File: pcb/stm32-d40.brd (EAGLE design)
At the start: 57.1 x 17.8 mm, 33 parts, among them IC1 TODO AMIS30663CANG2G, IC2 STM32F103C8, J1 DIP-40, Q2 8MHz, SW1 KSS-2EG4430, SW2 KSS-2EG4430, X1 DG3XX-03-3.5

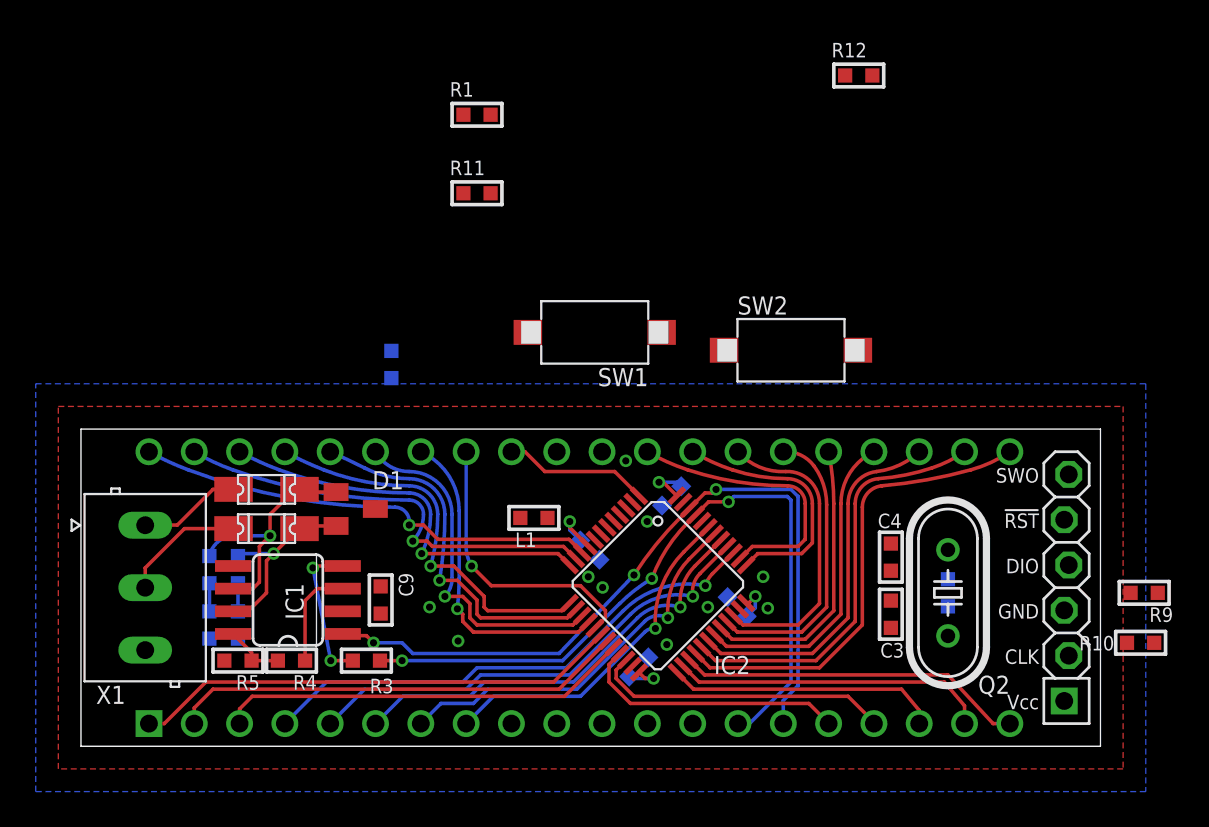
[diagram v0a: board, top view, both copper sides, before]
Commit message: DIP40 CAN ready
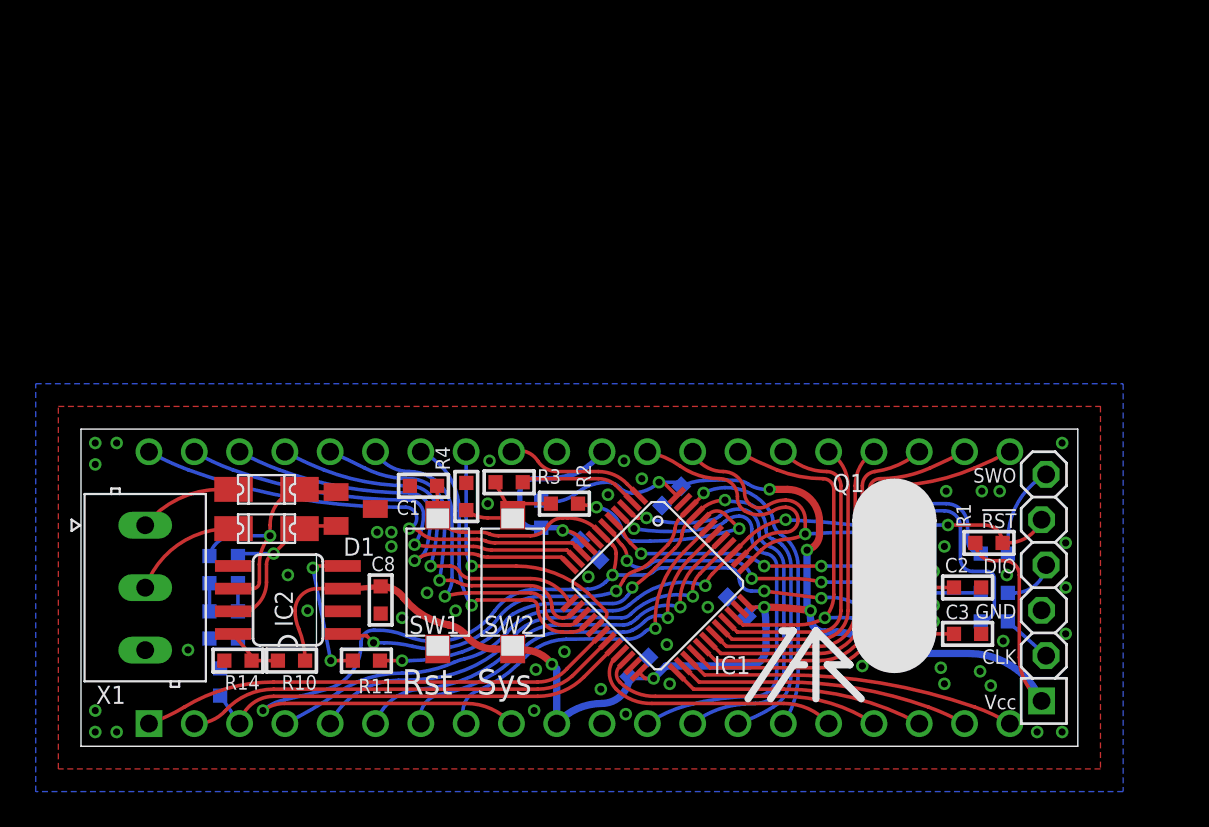
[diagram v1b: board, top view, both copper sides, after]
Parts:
- removed C11: 560pF, rc-master-smd:C0603
- removed Q2: 8MHz, discrete:HC49/S
- added C1: 0.1, rc-master-smd:C0603
- added C2: 22pF, rc-master-smd:C0603
- added Q1: 8MHz, discrete:HC49/S
- added R13: 100, rc-master-smd:R0603
- added R14: NC, rc-master-smd:R0603
- added U$: LOGO, logo:TT_LOGO
- C4: value 22pF -> 0.1
- C9: value 0.1 -> 560pF
- IC1: value TODO AMIS30663CANG2G -> STM32F103C8; device interfaces:SO08 -> stm32:LQFP48
- IC2: value STM32F103C8 -> TODO AMIS30663CANG2G; device stm32:LQFP48 -> interfaces:SO08
- R10: value 10K -> 0
- R11: value 2.2K -> 100
- R12, R8, R9: value 10K -> 100
- R2: value 1M -> 10K
- R3, R6: value 100 -> 10K
- R4: value 0 -> 2.2K
- R5: value NC -> 1M
- moved R10 47.6 mm to (11.8, 4.80)
- moved R12 44.5 mm to (8.80, 9.90), flipped to the bottom, turned to 90 degrees
- moved R7 44.1 mm to (51.2, 7.00), turned to 180 degrees
- moved R1 37.4 mm to (50.9, 11.4), turned to 180 degrees
- moved R5 37.1 mm to (45.6, 9.60), flipped to the bottom, turned to 270 degrees
- moved R8 36.1 mm to (51.2, 8.60), turned to 180 degrees
- moved R11 26.9 mm to (16.0, 4.80), turned to 180 degrees
- moved R2 22.1 mm to (27.1, 13.6), flipped to the top, turned to 0 degrees
- moved IC1 20.8 mm to (32.3, 9.09), turned to 225 degrees
- moved IC2 20.8 mm to (11.6, 8.20), turned to 90 degrees
- moved SW2 20.3 mm to (24.2, 9.20), turned to 90 degrees
- moved C8 17.3 mm to (16.8, 8.20), flipped to the top, turned to 270 degrees
- moved C4 16.9 mm to (28.5, 11.0), flipped to the bottom, turned to 225 degrees
- moved SW1 16.5 mm to (20.0, 9.20), turned to 90 degrees
- moved R4 13.4 mm to (21.6, 14.0), turned to 270 degrees
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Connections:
- new net N$2: R7.2, SWD1.2
- new net N$3: R8.2, SWD1.4
- new net N$4: R9.2, SWD1.6
- net !RESET: now also C1.1, IC1.7, R1.1; no longer IC2.7, R12.1
- net +3V3: now also C7.1, IC1.24, IC1.36, IC1.48, IC2.3, R1.2, R10.1; no longer C9.1, IC1.3, IC2.24, IC2.36, IC2.48, R10.2, R12.2, R4.1, R9.2
- net AVCC: now also C4.1, IC1.9; no longer C7.1, IC2.9
- net BOOT0: now also IC1.44, R2.2; no longer IC2.44, R1.2
- net CAN_CTRL: now also IC2.8, R10.2, R14.2; no longer IC1.8, R4.2, R5.2
- net GND: now also C1.2, C2.2, IC1.23, IC1.35, IC1.47, IC1.8, IC2.2, R14.1, R4.1, R6.2; no longer C11.2, IC1.2, IC2.23, IC2.35, IC2.47, IC2.8, R11.1, R5.1, R8.2
- net N$1: now also R2.1, R3.1, R4.2; no longer R1.1, R11.2
- net N$51: now also IC2.7, R12.2; no longer IC1.7, R6.2
- net N$52: now also IC2.6, R13.2; no longer IC1.6, R7.2
- net N$54: now also C10.1, R13.1; no longer C11.1, R7.1
- net N$55: now also C9.1, R12.1; no longer C10.1, R6.1
- net N$7: now also IC2.4, R11.2; no longer IC1.4, R3.2
- net OSC_IN: now also C2.1, IC1.5, Q1.1, R5.1; no longer C3.1, IC2.5, Q2.1, R2.1
- net OSC_OUT: now also C3.1, IC1.6, Q1.2, R5.2; no longer C4.1, IC2.6, Q2.2, R2.2
- net PA0: now also IC1.10; no longer IC2.10
- net PA1: now also IC1.11; no longer IC2.11
- net PA10/RXD1: now also IC1.31; no longer IC2.31
- net PA11/USBDM: now also IC1.32; no longer IC2.32
- net PA12/USBDP: now also IC1.33; no longer IC2.33
- net PA13/SWDIO: now also IC1.34, R8.1; no longer IC2.34, SWD1.4
- net PA14/SWCLK: now also IC1.37, R7.1; no longer IC2.37, SWD1.2
- net PA15: now also IC1.38; no longer IC2.38
- net PA2: now also IC1.12; no longer IC2.12
- net PA3: now also IC1.13; no longer IC2.13
- net PA4: now also IC1.14; no longer IC2.14
- net PA5: now also IC1.15; no longer IC2.15
- net PA6: now also IC1.16; no longer IC2.16
- net PA7: now also IC1.17; no longer IC2.17
- net PA8: now also IC1.29; no longer IC2.29
- net PA9/TXD1: now also IC1.30; no longer IC2.30
- net PB0: now also IC1.18; no longer IC2.18
- net PB1: now also IC1.19; no longer IC2.19
- net PB10: now also IC1.21; no longer IC2.21
- net PB11: now also IC1.22; no longer IC2.22
- net PB12: now also IC1.25; no longer IC2.25
- net PB13: now also IC1.26; no longer IC2.26
- net PB14: now also IC1.27; no longer IC2.27
- net PB15: now also IC1.28; no longer IC2.28
- net PB2: now also IC1.20, R6.1; no longer IC2.20, R8.1
- net PB3/SWO: now also IC1.39, R9.1; no longer IC2.39, SWD1.6
- net PB4: now also IC1.40; no longer IC2.40
- net PB5: now also IC1.41; no longer IC2.41
- net PB6/SCL1: now also IC1.42; no longer IC2.42, R9.1
- net PB7/SDA1: now also IC1.43; no longer IC2.43, R10.1
- net PB8/CANRX: now also IC1.45, R11.1; no longer IC2.45, R3.1
- net PB9/CANTX: now also IC1.46, IC2.1; no longer IC1.1, IC2.46
- net PC13: now also IC1.2, R3.2; no longer IC2.2
- net PC14/OSC32_IN: now also IC1.3; no longer IC2.3
- net PC15/OSC32_OUT: now also IC1.4; no longer IC2.4
- net VBAT: now also IC1.1; no longer IC2.1
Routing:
- net !RESET: track 0.00 -> 81.8 mm, vias 0 -> 5
- net +3V3: track 12.8 -> 92.7 mm, vias 3 -> 7
- net PC15/OSC32_OUT: track 0.00 -> 24.8 mm, vias 0 -> 1
- net OSC_IN: track 0.00 -> 24.1 mm, vias 0 -> 3
- net OSC_OUT: track 0.00 -> 23.3 mm, vias 0 -> 3
- net PC14/OSC32_IN: track 0.00 -> 22.9 mm, vias 0 -> 1
- net PB3/SWO: track 28.9 -> 44.1 mm, vias 1 -> 2
- net PA14/SWCLK: track 14.0 -> 28.7 mm, vias 0 -> 1
- net PA13/SWDIO: track 16.6 -> 29.3 mm, vias 0 -> 1
- net BOOT0: track 0.00 -> 12.4 mm, vias 0 -> 2
- net AVCC: track 3.14 -> 12.2 mm
- net N$1: track 0.00 -> 7.79 mm
- net PC13: track 0.00 -> 6.71 mm
- net N$4: track 0.00 -> 5.02 mm
- net PB9/CANTX: track 43.3 -> 40.3 mm
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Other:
- board size 57.1 x 17.8 mm -> 55.9 x 17.8 mm
- board text added: "!RST"
- board text added: "+3V3"
- board text added: "AVCC"
- board text added: "CAN"
- board text added: "CANARM"
- board text added: "GND"
- board text added: "H+"
- board text added: "L-"
- board text added: "PA0"
- board text added: "PA1"
- board text added: "PA10"
- board text added: "PA11"
- board text added: "PA12"
- board text added: "PA13"
- board text added: "PA14"
- board text added: "PA15"
- board text added: "PA2"
- board text added: "PA3"
- board text added: "PA4"
- board text added: "PA5"
- board text added: "PA6"
- board text added: "PA7"
- board text added: "PA8"
- board text added: "PA9"
- board text added: "PB0"
- board text added: "PB1"
- board text added: "PB10"
- board text added: "PB11"
- board text added: "PB12"
- board text added: "PB13"
- board text added: "PB14"
- board text added: "PB15"
- board text added: "PB2"
- board text added: "PB3"
- board text added: "PB4"
- board text added: "PB5"
- board text added: "PB6"
- board text added: "PB7"
- board text added: "PB8"
- board text added: "PB9"
- board text added: "PC14"
- board text added: "PC15"
- board text added: "Rev.13A"
- board text added: "Rst"
- board text added: "Sys"
- board text added: "Vbat"
- board text added: "i@tuxotronic.org"

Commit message: some wire fixes, add LED
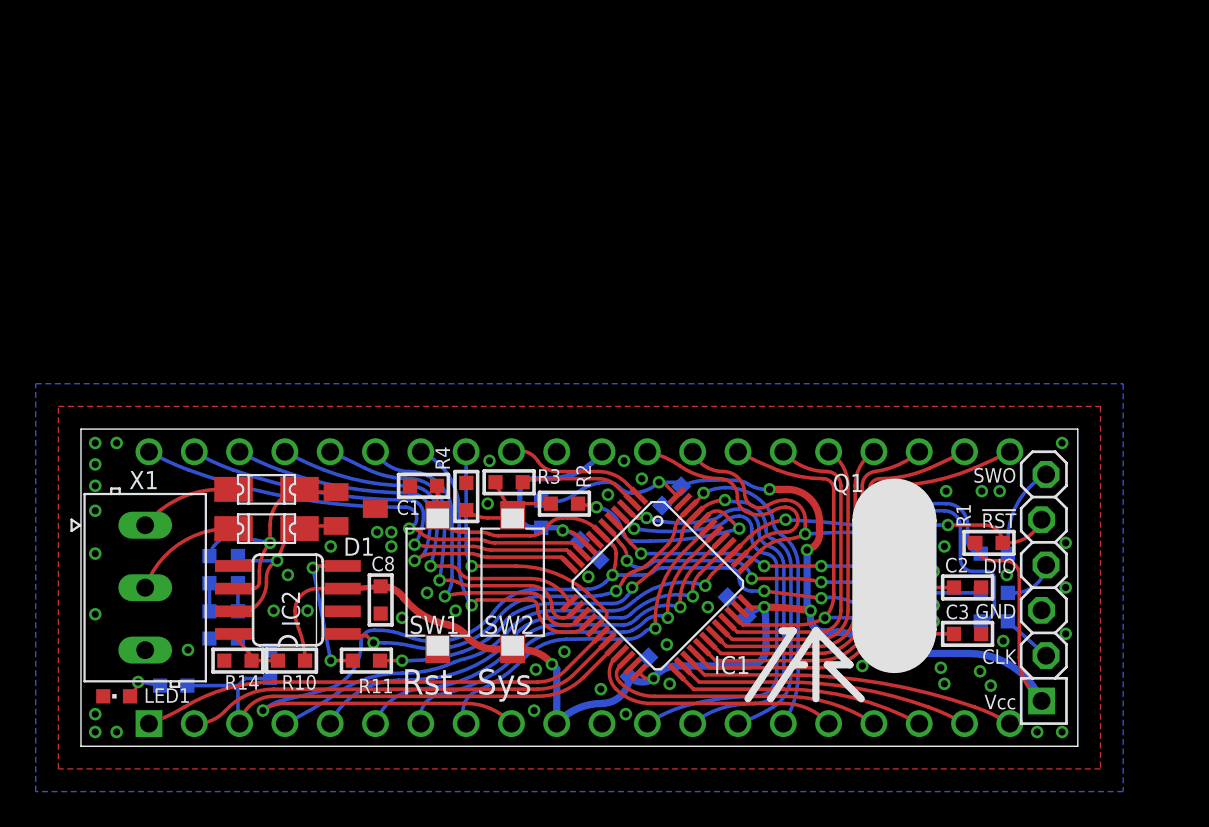
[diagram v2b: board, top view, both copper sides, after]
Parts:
- added LED1: (no value), led:CHIPLED_0603
- added R15: 330, rc-master-smd:R0603
- moved R6 2.97 mm to (10.6, 4.60)
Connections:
- new net N$5: LED1.A, R15.2
- net GND: now also LED1.C
- net PB2: now also R15.1
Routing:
- net PB2: track 24.3 -> 29.4 mm
- net N$5: track 0.00 -> 2.20 mm, vias 0 -> 1
